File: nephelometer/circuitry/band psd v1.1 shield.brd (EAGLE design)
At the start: 88 x 49 mm, 63 parts, among them IC1 LMC6484P, IC2 LM555N, IC3 74HCT74N, IC4 4044N, T1 2N2222, T2 2N2222, U1 MAX4544, U4 MotA

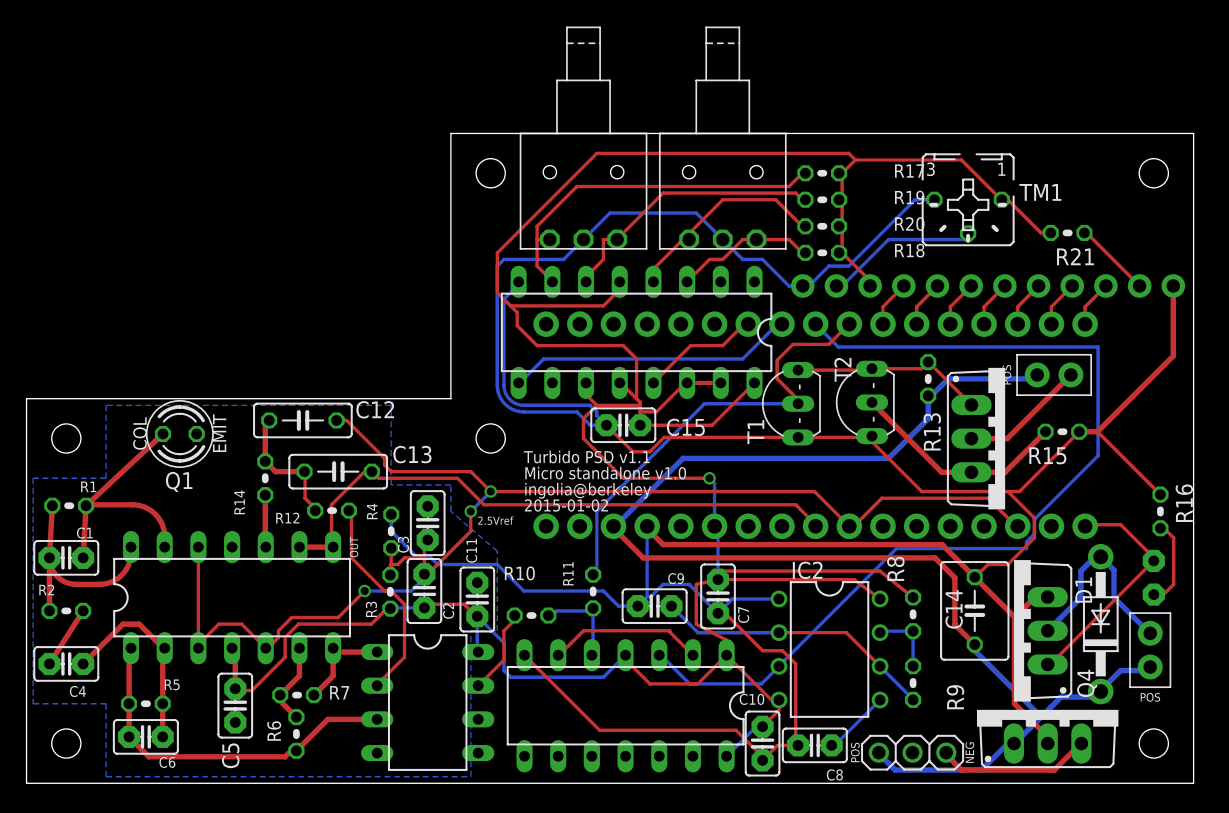
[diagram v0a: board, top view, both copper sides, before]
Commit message: Updated to use MCP3301 for ADC on stand-alone
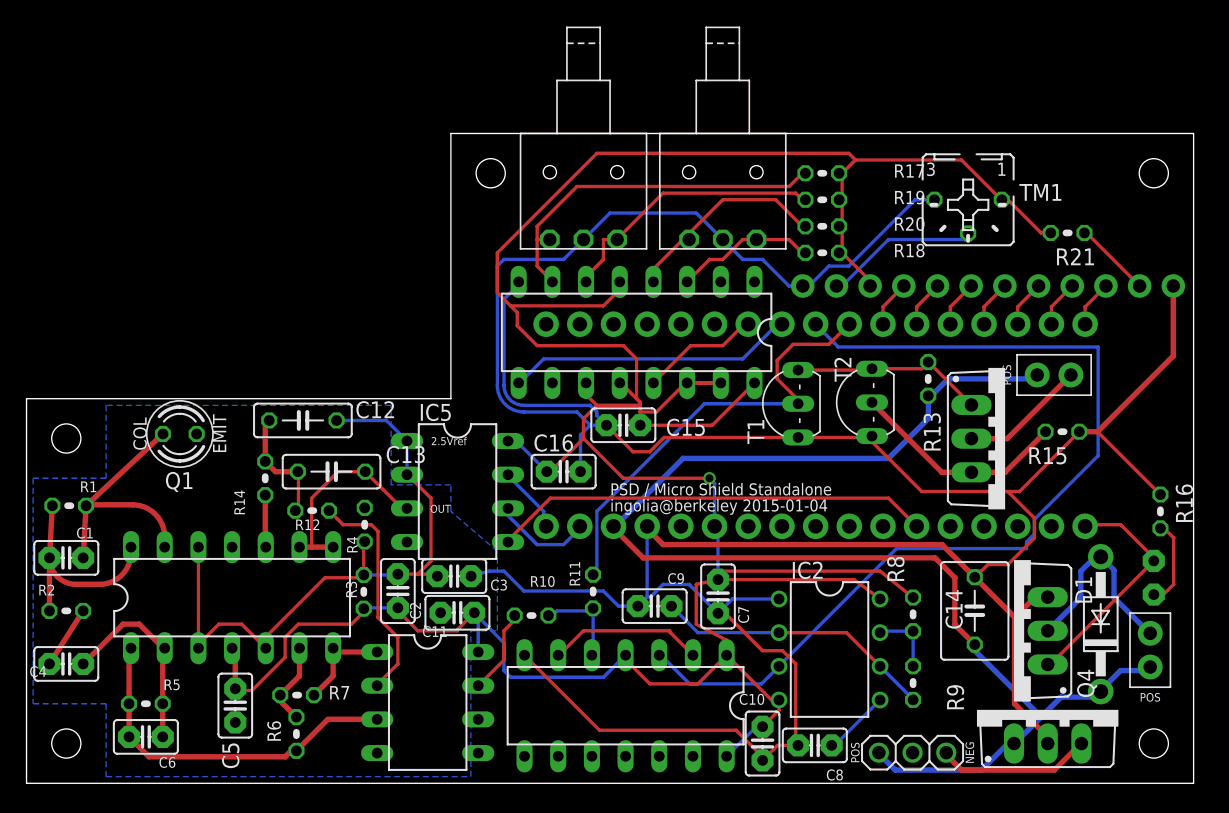
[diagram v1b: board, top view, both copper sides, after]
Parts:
- removed U$8: (no value), ingolia:M2MOUNT
- added C16: 100n, adafruit:C025-025X050
- added IC5: (no value), ingolia:DIL08
- moved C3 4.47 mm to (32.2, 21.6), turned to 0 degrees
- moved R4 2.06 mm to (25.5, 25.5)
- moved C2 2.00 mm to (28.0, 20.5)
- moved R3 2.00 mm to (25.4, 20.4)
- moved C11 1.80 mm to (32.5, 18.9), turned to 180 degrees
- moved R12 1.50 mm to (21.5, 26.6)
- moved C13 0.50 mm to (23.0, 29.5)
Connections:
- new net CS_ADC: IC5.5, U3.P$29
- new net MISO: IC5.6, U3.P$19
- new net SCK: IC5.7, U3.P$18
- net +5V: now also C16.1, IC5.8
- net 2.5V: now also IC5.1, IC5.2; no longer U3.P$27, U3.P$32
- net GND: now also C16.2, IC5.4
- net N$28: now also IC5.3; no longer U3.P$26
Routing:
- net 2.5V: track 102.5 -> 49.9 mm, vias 3 -> 0
- net CS_ADC: track 0.00 -> 33.1 mm
- net N$28: track 45.1 -> 15.4 mm
- net +5V: track 239.3 -> 248.7 mm
- net MISO: track 0.00 -> 7.77 mm
- net SCK: track 0.00 -> 5.08 mm
- net GND: track 271.0 -> 266.3 mm
- net N$6: track 16.1 -> 17.2 mm
- net N$27: track 9.76 -> 9.03 mm
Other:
- board text added: "PSD / Micro Shield Standalone ingolia@berkeley 2015-01-04"
- board text removed: "Turbido PSD v1.1 Micro standalone v1.0 ingolia@berkeley 2015-01-02"
